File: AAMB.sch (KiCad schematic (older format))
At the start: 7 parts, among them J1 Screw_Terminal_01x04, J2 PJRAS4X2U01X, J3 SPKR L, J4 SPKR R, J5 Screw_Terminal_01x03, J6 Screw_Terminal_01x03, J7 Conn_01x04

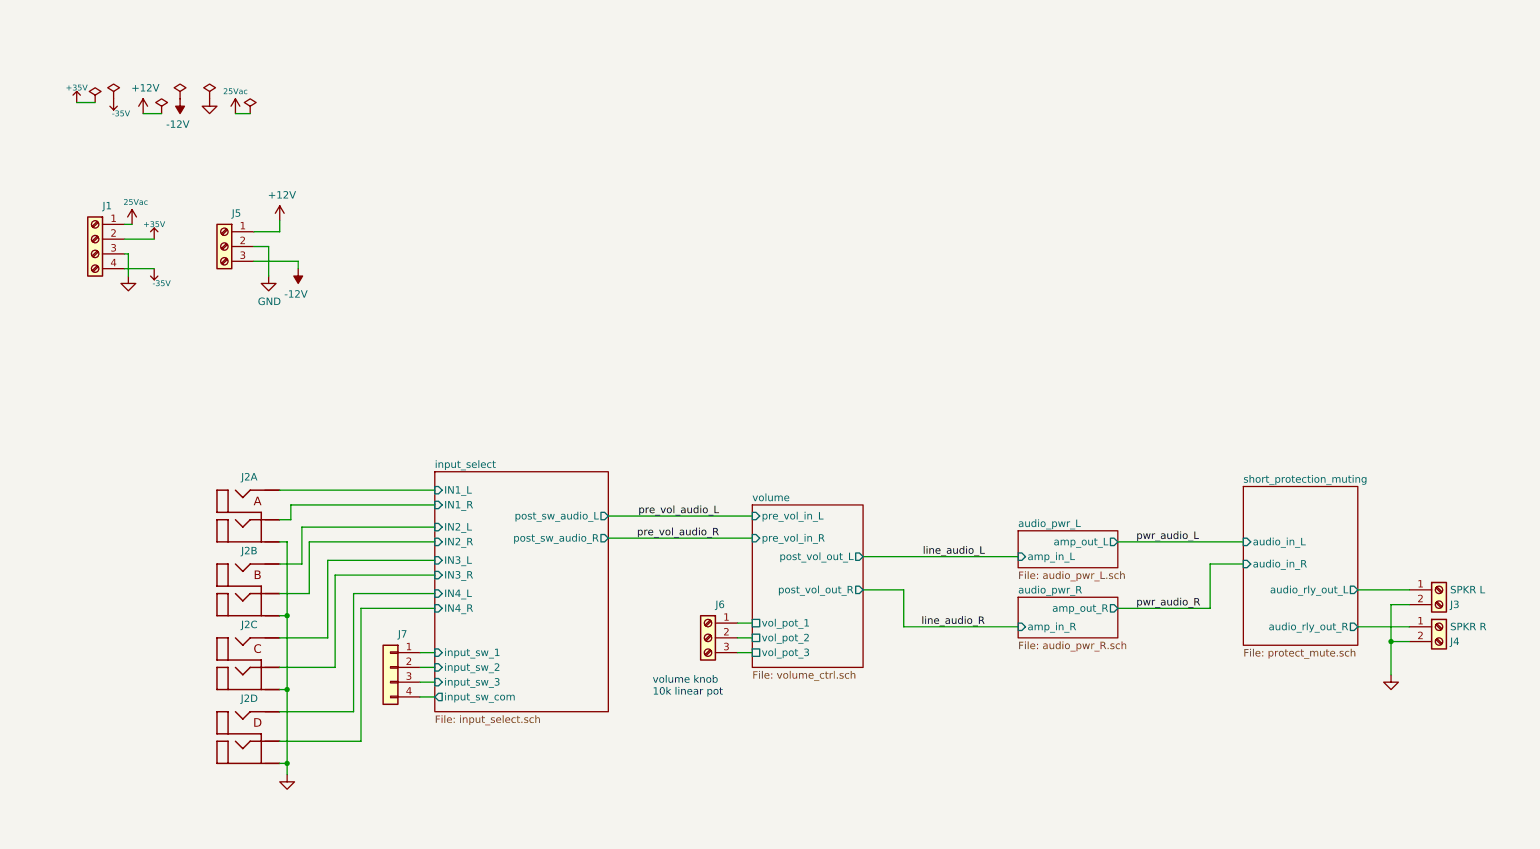
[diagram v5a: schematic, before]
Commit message: Added test points. Schematic cleanup.
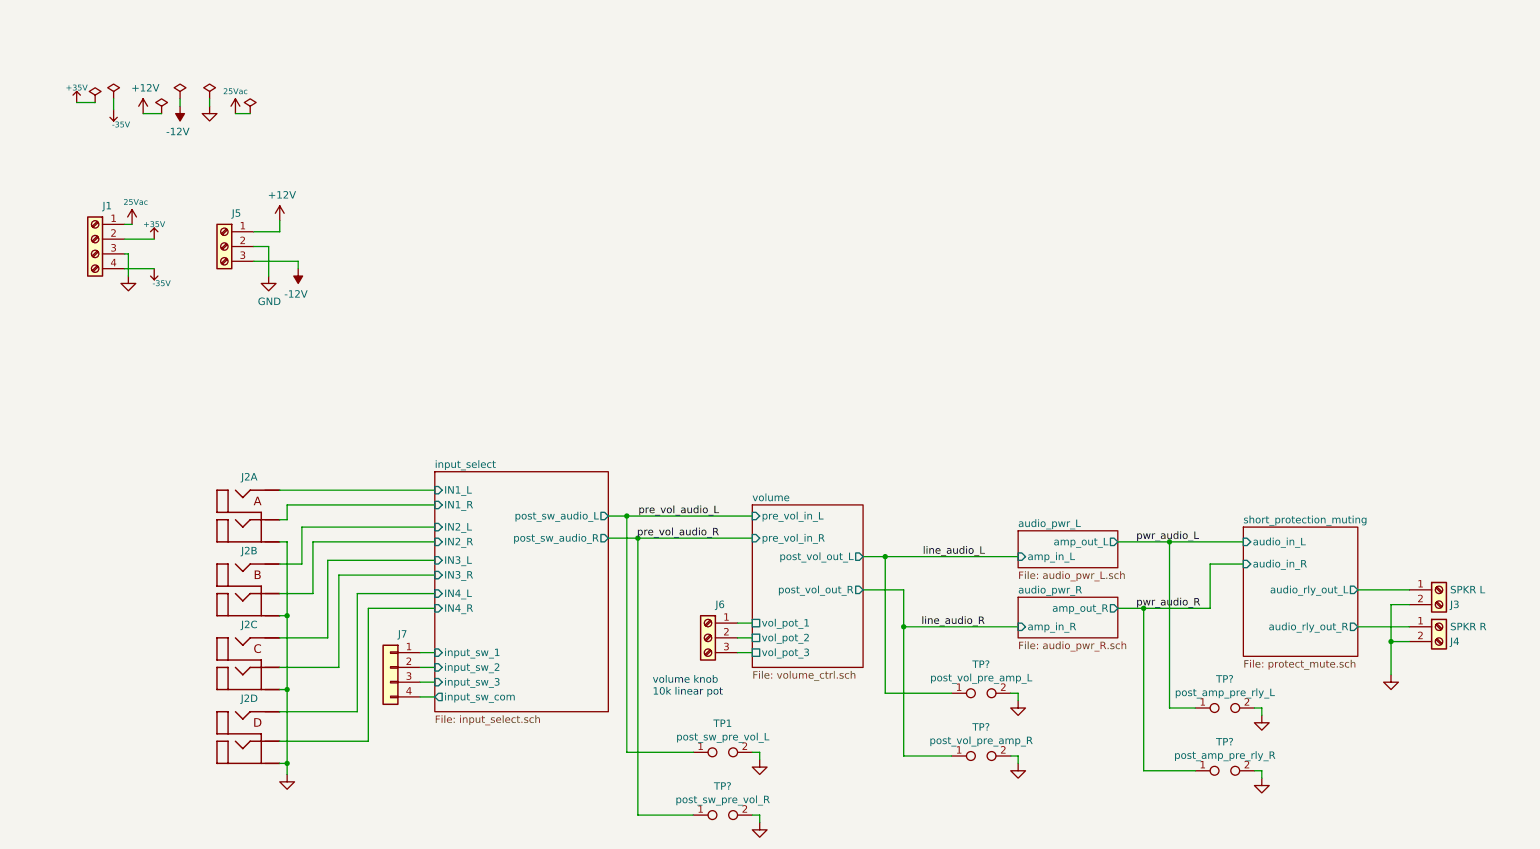
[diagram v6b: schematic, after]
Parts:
- added TP1: post_sw_pre_vol_L, TestPoint:TestPoint_Bridge_Pitch2.54mm_Drill1.0mm, symbol Connector:TestPoint_2Pole
- added TP?: post_sw_pre_vol_R, TestPoint:TestPoint_Bridge_Pitch2.54mm_Drill1.0mm, symbol Connector:TestPoint_2Pole
- added TP?: post_vol_pre_amp_L, TestPoint:TestPoint_Bridge_Pitch2.54mm_Drill1.0mm, symbol Connector:TestPoint_2Pole
- added TP?: post_vol_pre_amp_R, TestPoint:TestPoint_Bridge_Pitch2.54mm_Drill1.0mm, symbol Connector:TestPoint_2Pole
- added TP?: post_amp_pre_rly_L, TestPoint:TestPoint_Bridge_Pitch2.54mm_Drill1.0mm, symbol Connector:TestPoint_2Pole
- added TP?: post_amp_pre_rly_R, TestPoint:TestPoint_Bridge_Pitch2.54mm_Drill1.0mm, symbol Connector:TestPoint_2Pole
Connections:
- net GND: now also TP1.2, TP?.2, TP?.2, TP?.2, TP?.2, TP?.2
- net line_audio_L: now also TP?.1
- net line_audio_R: now also TP?.1
- net pre_vol_audio_L: now also TP1.1
- net pre_vol_audio_R: now also TP?.1
- net pwr_audio_L: now also TP?.1
- net pwr_audio_R: now also TP?.1

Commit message: Cleaning up user configs.
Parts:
- removed J7: Conn_01x04, symbol Connector_Generic:Conn_01x04
- added J7: Screw_Terminal_01x04, TerminalBlock_Phoenix:TerminalBlock_Phoenix_MKDS-1,5-4_1x04_P5.00mm_Horizontal, symbol Connector:Screw_Terminal_01x04
- J2: DigiKey (none) -> http://datasheets.diptrace.com/con_rca_jack/pjras4x2u__x_se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; Field4 http://datasheets.diptrace.com/con_rca_jack/pjras4x2u__x_se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 -> (none)
- J3, J4: DigiKey (none) -> https://www.digikey.com/product-detail/en/phoenix-contact/1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
- J5, J6: footprint (none) -> TerminalBlock_Phoenix:TerminalBlock_Phoenix_MKDS-1,5-3_1x03_P5.00mm_Horizontal
- gave numbers to parts that had none: 5
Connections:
- net input_select/input_sw_1: now also J7.1 (Pin_1)
- net input_select/input_sw_2: now also J7.2 (Pin_2)
- net input_select/input_sw_3: now also J7.3 (Pin_3)
- net input_select/input_sw_com: now also J7.4 (Pin_4)
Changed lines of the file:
@@
 F 1 "PJRAS4X2U01X" H 1525 3775 50  0001 L BNN
 F 2 "Connectors-amp:PJRAS4X2U01X" H 1525 3850 50  0001 L BNN
-F 3 "Switchcraft" H 1725 3600 50  0001 L BNN
-F 4 "http://datasheets.diptrace.com/con_rca_jack/pjras4x2u__x_series_cd.pdf" H 1525 3300 50  0001 L BNN "Field4"
+F 3 "" H 1725 3600 50  0001 L BNN
+F 4 "" H 1525 3300 50  0001 L BNN "Field4"
+F 5 "http://datasheets.diptrace.com/con_rca_jack/pjras4x2u__x_series_cd.pdf" H 1800 3500 50  0001 C CNN "DigiKey"
 	1    1800 3500
 	1    0    0    -1
@@
 F 1 "PJRAS4X2U01X" H 1525 4275 50  0001 L BNN
 F 2 "Connectors-amp:PJRAS4X2U01X" H 1525 4350 50  0001 L BNN
-F 3 "Switchcraft" H 1725 4100 50  0001 L BNN
-F 4 "http://datasheets.diptrace.com/con_rca_jack/pjras4x2u__x_series_cd.pdf" H 1525 3800 50  0001 L BNN "Field4"
+F 3 "" H 1725 4100 50  0001 L BNN
+F 4 "" H 1525 3800 50  0001 L BNN "Field4"
+F 5 "http://datasheets.diptrace.com/con_rca_jack/pjras4x2u__x_series_cd.pdf" H 1800 4000 50  0001 C CNN "DigiKey"
 	2    1800 4000
 	1    0    0    -1
@@
 F 1 "PJRAS4X2U01X" H 1525 4775 50  0001 L BNN
 F 2 "Connectors-amp:PJRAS4X2U01X" H 1525 4850 50  0001 L BNN
-F 3 "Switchcraft" H 1725 4600 50  0001 L BNN
-F 4 "http://datasheets.diptrace.com/con_rca_jack/pjras4x2u__x_series_cd.pdf" H 1525 4300 50  0001 L BNN "Field4"
+F 3 "" H 1725 4600 50  0001 L BNN
+F 4 "" H 1525 4300 50  0001 L BNN "Field4"
+F 5 "http://datasheets.diptrace.com/con_rca_jack/pjras4x2u__x_series_cd.pdf" H 1800 4500 50  0001 C CNN "DigiKey"
 	3    1800 4500
 	1    0    0    -1
@@
 F 1 "PJRAS4X2U01X" H 1525 5275 50  0001 L BNN
 F 2 "Connectors-amp:PJRAS4X2U01X" H 1525 5350 50  0001 L BNN
-F 3 "Switchcraft" H 1725 5100 50  0001 L BNN
-F 4 "http://datasheets.diptrace.com/con_rca_jack/pjras4x2u__x_series_cd.pdf" H 1525 4800 50  0001 L BNN "Field4"
+F 3 "" H 1725 5100 50  0001 L BNN
+F 4 "" H 1525 4800 50  0001 L BNN "Field4"
+F 5 "http://datasheets.diptrace.com/con_rca_jack/pjras4x2u__x_series_cd.pdf" H 1800 5000 50  0001 C CNN "DigiKey"
 	4    1800 5000
 	1    0    0    -1
@@
 F 1 "SPKR L" H 9875 3925 50  0000 L CNN
 F 2 "TerminalBlock_Phoenix:TerminalBlock_Phoenix_MKDS-1,5-2_1x02_P5.00mm_Horizontal" H 9800 3925 50  0001 C CNN
-F 3 "https://www.digikey.com/product-detail/en/phoenix-contact/1715022/277-1258-ND/260626" H 9800 3925 50  0001 C CNN
+F 3 "" H 9800 3925 50  0001 C CNN
+F 4 "https://www.digikey.com/product-detail/en/phoenix-contact/1715022/277-1258-ND/260626" H 9800 3925 50  0001 C CNN "DigiKey"
 	1    9800 3925
 	1    0    0    -1
@@
 F 1 "SPKR R" H 9875 4175 50  0000 L CNN
 F 2 "TerminalBlock_Phoenix:TerminalBlock_Phoenix_MKDS-1,5-2_1x02_P5.00mm_Horizontal" H 9800 4175 50  0001 C CNN
-F 3 "https://www.digikey.com/product-detail/en/phoenix-contact/1715022/277-1258-ND/260626" H 9800 4175 50  0001 C CNN
+F 3 "" H 9800 4175 50  0001 C CNN
+F 4 "https://www.digikey.com/product-detail/en/phoenix-contact/1715022/277-1258-ND/260626" H 9800 4175 50  0001 C CNN "DigiKey"
 	1    9800 4175
 	1    0    0    -1
@@
 F 0 "J5" H 1493 1825 50  0000 C CNN
 F 1 "Screw_Terminal_01x03" H 1493 1826 50  0001 C CNN
-F 2 "" H 1575 1600 50  0001 C CNN
+F 2 "TerminalBlock_Phoenix:TerminalBlock_Phoenix_MKDS-1,5-3_1x03_P5.00mm_Horizontal" H 1575 1600 50  0001 C CNN
 F 3 "~" H 1575 1600 50  0001 C CNN
 	1    1575 1600
@@
 F 0 "J6" H 4768 4475 50  0000 C CNN
 F 1 "Screw_Terminal_01x03" H 4768 4476 50  0001 C CNN
-F 2 "" H 4850 4250 50  0001 C CNN
+F 2 "TerminalBlock_Phoenix:TerminalBlock_Phoenix_MKDS-1,5-3_1x03_P5.00mm_Horizontal" H 4850 4250 50  0001 C CNN
 F 3 "~" H 4850 4250 50  0001 C CNN
 	1    4850 4250
@@
 $EndComp
 $Comp
-L Connector_Generic:Conn_01x04 J7
-U 1 1 5E2AFFDD
-P 2700 4450
-F 0 "J7" H 2618 4675 50  0000 C CNN
-F 1 "Conn_01x04" H 2618 4676 50  0001 C CNN
-F 2 "" H 2700 4450 50  0001 C CNN
-F 3 "~" H 2700 4450 50  0001 C CNN
-	1    2700 4450
-	-1   0    0    -1
-$EndComp
-$Comp
 L power:PWR_FLAG #FLG0103
 U 1 1 5E2EA3BE
@@
 P 1275 650
 F 0 "#PWR0115" H 1275 750 50  0001 C CNN
-F 1 "-12V" H 1290 823 50  0000 C CNN
+F 1 "-12V" H 1300 800 39  0000 C CNN
 F 2 "" H 1275 650 50  0001 C CNN
 F 3 "" H 1275 650 50  0001 C CNN
@@
 P 1025 700
 F 0 "#PWR0116" H 1025 550 50  0001 C CNN
-F 1 "+12V" H 1040 873 50  0000 C CNN
+F 1 "+12V" H 1000 850 39  0000 C CNN
 F 2 "" H 1025 700 50  0001 C CNN
 F 3 "" H 1025 700 50  0001 C CNN
@@
 P 1475 650
 F 0 "#PWR0121" H 1475 400 50  0001 C CNN
-F 1 "GND" H 1475 500 50  0001 C CNN
+F 1 "GND" H 1475 500 39  0000 C CNN
 F 2 "" H 1475 650 50  0001 C CNN
 F 3 "" H 1475 650 50  0001 C CNN
@@
 L power:25Vac #PWR0124
 U 1 1 5E3BCE97
-P 950 1450
-F 0 "#PWR0124" H 950 1300 50  0001 C CNN
-F 1 "25Vac" H 975 1600 39  0000 C CNN
-F 2 "" H 950 1450 50  0001 C CNN
-F 3 "" H 950 1450 50  0001 C CNN
-	1    950  1450
+P 950 1375
+F 0 "#PWR0124" H 950 1225 50  0001 C CNN
+F 1 "25Vac" H 975 1525 39  0000 C CNN
+F 2 "" H 950 1375 50  0001 C CNN
+F 3 "" H 950 1375 50  0001 C CNN
+	1    950  1375
 	1    0    0    -1
 $EndComp
@@
 $EndComp
 $Comp
-L power:GND #PWR?
+L power:GND #PWR06
 U 1 1 5E4720E6
 P 5200 5075
-F 0 "#PWR?" H 5200 4825 50  0001 C CNN
+F 0 "#PWR06" H 5200 4825 50  0001 C CNN
 F 1 "GND" H 5200 4925 50  0001 C CNN
 F 2 "" H 5200 5075 50  0001 C CNN
@@
 	5200 5025 5150 5025
 $Comp
-L Connector:TestPoint_2Pole TP?
+L Connector:TestPoint_2Pole TP2
 U 1 1 5E475BA6
 P 4950 5450
-F 0 "TP?" H 4950 5645 50  0000 C CNN
+F 0 "TP2" H 4950 5645 50  0000 C CNN
 F 1 "post_sw_pre_vol_R" H 4950 5554 50  0000 C CNN
 F 2 "TestPoint:TestPoint_Bridge_Pitch2.54mm_Drill1.0mm" H 4950 5450 50  0001 C CNN
@@
 $EndComp
 $Comp
-L power:GND #PWR?
+L power:GND #PWR07
 U 1 1 5E475BAC
 P 5200 5500
-F 0 "#PWR?" H 5200 5250 50  0001 C CNN
+F 0 "#PWR07" H 5200 5250 50  0001 C CNN
 F 1 "GND" H 5200 5350 50  0001 C CNN
 F 2 "" H 5200 5500 50  0001 C CNN
@@
 	4375 3575 4375 5450
 $Comp
-L Connector:TestPoint_2Pole TP?
+L Connector:TestPoint_2Pole TP3
 U 1 1 5E4977C7
 P 6700 4625
-F 0 "TP?" H 6700 4820 50  0000 C CNN
+F 0 "TP3" H 6700 4820 50  0000 C CNN
 F 1 "post_vol_pre_amp_L" H 6700 4729 50  0000 C CNN
 F 2 "TestPoint:TestPoint_Bridge_Pitch2.54mm_Drill1.0mm" H 6700 4625 50  0001 C CNN
@@
 $EndComp
 $Comp
-L power:GND #PWR?
+L power:GND #PWR024
 U 1 1 5E4977CD
 P 6950 4675
-F 0 "#PWR?" H 6950 4425 50  0001 C CNN
+F 0 "#PWR024" H 6950 4425 50  0001 C CNN
 F 1 "GND" H 6950 4525 50  0001 C CNN
 F 2 "" H 6950 4675 50  0001 C CNN
@@
 	6950 4625 6900 4625
 $Comp
-L Connector:TestPoint_2Pole TP?
+L Connector:TestPoint_2Pole TP4
 U 1 1 5E4977D5
 P 6700 5050
-F 0 "TP?" H 6700 5245 50  0000 C CNN
+F 0 "TP4" H 6700 5245 50  0000 C CNN
 F 1 "post_vol_pre_amp_R" H 6700 5154 50  0000 C CNN
 F 2 "TestPoint:TestPoint_Bridge_Pitch2.54mm_Drill1.0mm" H 6700 5050 50  0001 C CNN
@@
 $EndComp
 $Comp
-L power:GND #PWR?
+L power:GND #PWR025
 U 1 1 5E4977DB
 P 6950 5100
-F 0 "#PWR?" H 6950 4850 50  0001 C CNN
+F 0 "#PWR025" H 6950 4850 50  0001 C CNN
 F 1 "GND" H 6950 4950 50  0001 C CNN
 F 2 "" H 6950 5100 50  0001 C CNN
@@
 	6950 5050 6900 5050
 $Comp
-L Connector:TestPoint_2Pole TP?
+L Connector:TestPoint_2Pole TP5
 U 1 1 5E49F891
 P 8350 4725
-F 0 "TP?" H 8350 4920 50  0000 C CNN
+F 0 "TP5" H 8350 4920 50  0000 C CNN
 F 1 "post_amp_pre_rly_L" H 8350 4829 50  0000 C CNN
 F 2 "TestPoint:TestPoint_Bridge_Pitch2.54mm_Drill1.0mm" H 8350 4725 50  0001 C CNN
@@
 $EndComp
 $Comp
-L power:GND #PWR?
+L power:GND #PWR027
 U 1 1 5E49F897
 P 8600 4775
-F 0 "#PWR?" H 8600 4525 50  0001 C CNN
+F 0 "#PWR027" H 8600 4525 50  0001 C CNN
 F 1 "GND" H 8600 4625 50  0001 C CNN
 F 2 "" H 8600 4775 50  0001 C CNN
@@
 	8600 4725 8550 4725
 $Comp
-L Connector:TestPoint_2Pole TP?
+L Connector:TestPoint_2Pole TP6
 U 1 1 5E49F89F
 P 8350 5150
-F 0 "TP?" H 8350 5345 50  0000 C CNN
+F 0 "TP6" H 8350 5345 50  0000 C CNN
 F 1 "post_amp_pre_rly_R" H 8350 5254 50  0000 C CNN
 F 2 "TestPoint:TestPoint_Bridge_Pitch2.54mm_Drill1.0mm" H 8350 5150 50  0001 C CNN
@@
 $EndComp
 $Comp
-L power:GND #PWR?
+L power:GND #PWR029
 U 1 1 5E49F8A5
 P 8600 5200
-F 0 "#PWR?" H 8600 4950 50  0001 C CNN
+F 0 "#PWR029" H 8600 4950 50  0001 C CNN
 F 1 "GND" H 8600 5050 50  0001 C CNN
 F 2 "" H 8600 5200 50  0001 C CNN
@@
 Wire Wire Line
 	1475 650  1475 600
+Wire Wire Line
+	950  1375 950  1450
+$Comp
+L Connector:Screw_Terminal_01x04 J7
+U 1 1 5E6424F4
+P 2700 4450
+F 0 "J7" H 2618 4675 50  0000 C CNN
+F 1 "Screw_Terminal_01x04" H 2618 4676 50  0001 C CNN
+F 2 "TerminalBlock_Phoenix:TerminalBlock_Phoenix_MKDS-1,5-4_1x04_P5.00mm_Horizontal" H 2700 4450 50  0001 C CNN
+F 3 "~" H 2700 4450 50  0001 C CNN
+	1    2700 4450
+	-1   0    0    -1
+$EndComp
 $EndSCHEMATC

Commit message: Testing branch. Pulled parts into layout.
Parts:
- TP1, TP2, TP3, TP4, TP5, TP6: footprint TestPoint:TestPoint_Bridge_Pitch2.54mm_Drill1.0mm -> TestPoint:TestPoint_2Pads_Pitch2.54mm_Drill0.8mm
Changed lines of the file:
@@
 F 0 "TP1" H 4950 5220 50  0000 C CNN
 F 1 "post_sw_pre_vol_L" H 4950 5129 50  0000 C CNN
-F 2 "TestPoint:TestPoint_Bridge_Pitch2.54mm_Drill1.0mm" H 4950 5025 50  0001 C CNN
+F 2 "TestPoint:TestPoint_2Pads_Pitch2.54mm_Drill0.8mm" H 4950 5025 50  0001 C CNN
 F 3 "~" H 4950 5025 50  0001 C CNN
 	1    4950 5025
@@
 F 0 "TP2" H 4950 5645 50  0000 C CNN
 F 1 "post_sw_pre_vol_R" H 4950 5554 50  0000 C CNN
-F 2 "TestPoint:TestPoint_Bridge_Pitch2.54mm_Drill1.0mm" H 4950 5450 50  0001 C CNN
+F 2 "TestPoint:TestPoint_2Pads_Pitch2.54mm_Drill0.8mm" H 4950 5450 50  0001 C CNN
 F 3 "~" H 4950 5450 50  0001 C CNN
 	1    4950 5450
@@
 F 0 "TP3" H 6700 4820 50  0000 C CNN
 F 1 "post_vol_pre_amp_L" H 6700 4729 50  0000 C CNN
-F 2 "TestPoint:TestPoint_Bridge_Pitch2.54mm_Drill1.0mm" H 6700 4625 50  0001 C CNN
+F 2 "TestPoint:TestPoint_2Pads_Pitch2.54mm_Drill0.8mm" H 6700 4625 50  0001 C CNN
 F 3 "~" H 6700 4625 50  0001 C CNN
 	1    6700 4625
@@
 F 0 "TP4" H 6700 5245 50  0000 C CNN
 F 1 "post_vol_pre_amp_R" H 6700 5154 50  0000 C CNN
-F 2 "TestPoint:TestPoint_Bridge_Pitch2.54mm_Drill1.0mm" H 6700 5050 50  0001 C CNN
+F 2 "TestPoint:TestPoint_2Pads_Pitch2.54mm_Drill0.8mm" H 6700 5050 50  0001 C CNN
 F 3 "~" H 6700 5050 50  0001 C CNN
 	1    6700 5050
@@
 F 0 "TP5" H 8350 4920 50  0000 C CNN
 F 1 "post_amp_pre_rly_L" H 8350 4829 50  0000 C CNN
-F 2 "TestPoint:TestPoint_Bridge_Pitch2.54mm_Drill1.0mm" H 8350 4725 50  0001 C CNN
+F 2 "TestPoint:TestPoint_2Pads_Pitch2.54mm_Drill0.8mm" H 8350 4725 50  0001 C CNN
 F 3 "~" H 8350 4725 50  0001 C CNN
 	1    8350 4725
@@
 F 0 "TP6" H 8350 5345 50  0000 C CNN
 F 1 "post_amp_pre_rly_R" H 8350 5254 50  0000 C CNN
-F 2 "TestPoint:TestPoint_Bridge_Pitch2.54mm_Drill1.0mm" H 8350 5150 50  0001 C CNN
+F 2 "TestPoint:TestPoint_2Pads_Pitch2.54mm_Drill0.8mm" H 8350 5150 50  0001 C CNN
 F 3 "~" H 8350 5150 50  0001 C CNN
 	1    8350 5150
